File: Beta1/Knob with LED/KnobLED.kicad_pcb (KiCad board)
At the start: 2 copper layers, 197.9 x 41 mm, 116 parts, among them U0 APA102C, U1 APA102C, U10 APA102C, U1000 MCP3008T-I/SL, U11 APA102C, U12 APA102C, U13 APA102C, U14 APA102C, U15 APA102C, U2 APA102C, U3 APA102C, U4 APA102C, U5 APA102C, U6 APA102C, U7 APA102C, U8 APA102C, U9 APA102C

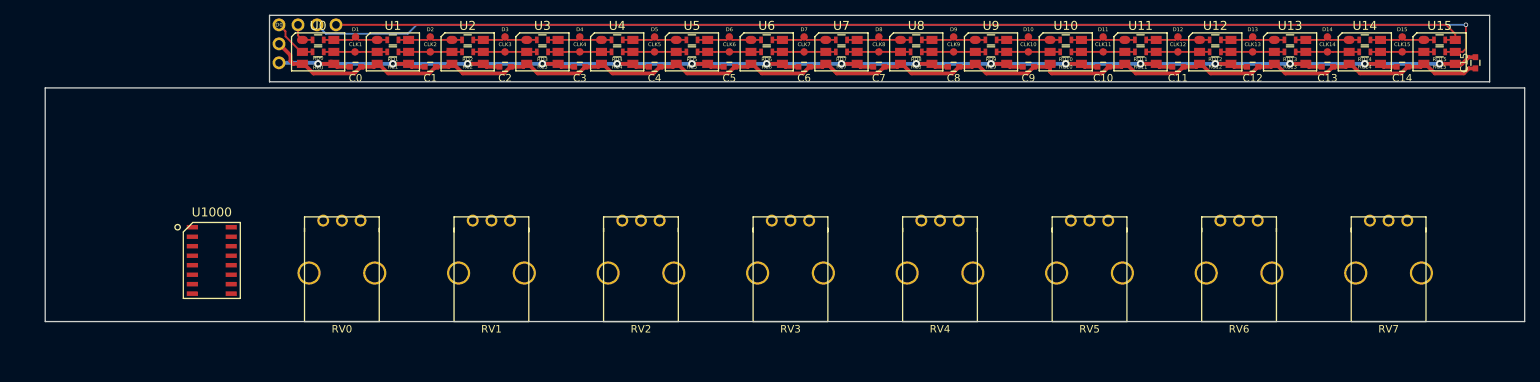
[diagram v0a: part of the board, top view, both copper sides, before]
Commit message: Fixed a math error and adjusted height of led board + component heights
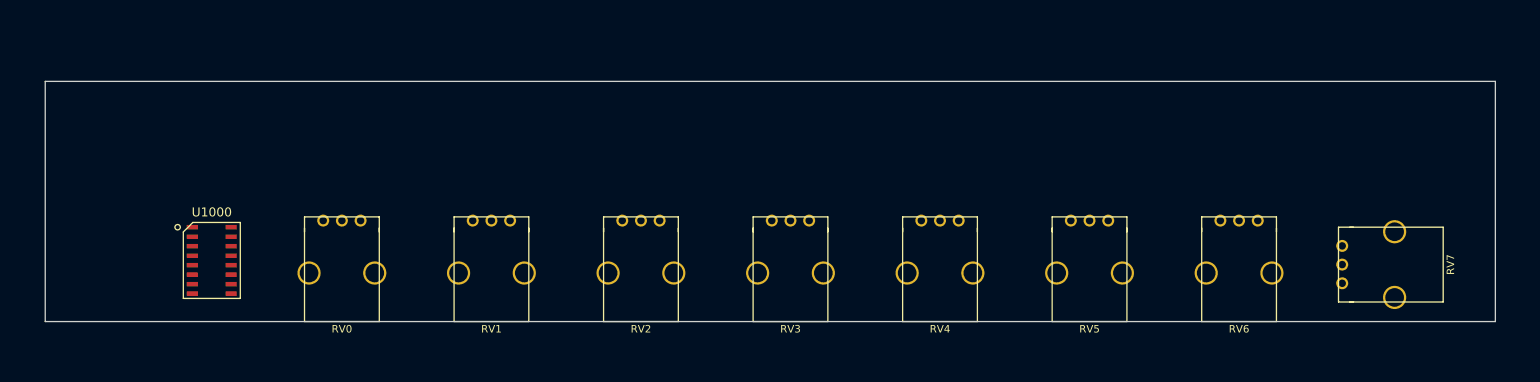
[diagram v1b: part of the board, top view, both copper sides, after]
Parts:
- removed C0, C1, C10, C11, C12, C13, C14, C15, C2, C3, C4, C5, C6, C7, C8, C9: 0.1u, Capacitors_SMD:C_0603
- removed CLK0, CLKOUT1, D0, DOUT1, GND0, VCC0: CONN_01X01, Liberry:single_0.1
- removed CLK1, CLK10, CLK11, CLK12, CLK13, CLK14, CLK15, CLK2, CLK3, CLK4, CLK5, CLK6, CLK7, CLK8, CLK9, D1, D10, D11, D12, D13, D14, D15, D2, D3, D4, D5, D6, D7, D8, D9: CONN_01X01, Liberry:TESTPAD
- removed RC0, RC1, RC10, RC11, RC12, RC13, RC14, RC15, RC2, RC3, RC4, RC5, RC6, RC7, RC8, RC9, RD0, RD1, RD10, RD11, RD12, RD13, RD14, RD15, RD2, RD3, RD4, RD5, RD6, RD7, RD8, RD9: ZERO, Resistors_SMD:R_0603
- removed U0, U1, U10, U11, U12, U13, U14, U15, U2, U3, U4, U5, U6, U7, U8, U9: APA102C, Liberry:PLCC6-1.6x4.2_LED
- moved RV7 3.60 mm to (177.0, -7.62), turned to 270 degrees
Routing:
- net +5V: track 227.1 -> 0.00 mm, vias 16 -> 0
- net GND: track 179.6 -> 0.00 mm
- net /LED_Strip/CLK16: track 160.8 -> 0.00 mm, vias 1 -> 0
- net /LED_Strip/D16: track 152.6 -> 0.00 mm
- net Net-(D1-Pad1): track 9.02 -> 0.00 mm
- net Net-(D3-Pad1): track 8.83 -> 0.00 mm
- net Net-(D2-Pad1): track 8.83 -> 0.00 mm
- net Net-(D9-Pad1): track 8.83 -> 0.00 mm
- net Net-(D7-Pad1): track 8.83 -> 0.00 mm
- net Net-(D6-Pad1): track 8.83 -> 0.00 mm
- net Net-(D5-Pad1): track 8.83 -> 0.00 mm
- net Net-(D15-Pad1): track 8.83 -> 0.00 mm
- net Net-(D14-Pad1): track 8.83 -> 0.00 mm
- net Net-(D13-Pad1): track 8.83 -> 0.00 mm
- net Net-(D11-Pad1): track 8.83 -> 0.00 mm
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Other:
- board size 197.9 x 41 mm -> 194 x 32.1 mm

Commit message: Duplicated row. Placed components and drill holes. Ready to be routed.
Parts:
- removed SPI_CS1: CONN_01X01, Liberry:single_0.1
- added C2: 0.1u, Capacitors_SMD:C_0603, F.Cu at (9.41, -9.34)
- added MISO2: CONN_01X01, Liberry:single_0.1, F.Cu at (7.62, -6.80)
- added REF**: 1pin, Connect:1pin, F.Cu at (3.00, -3.00)
- added REF**: 1pin, Connect:1pin, F.Cu at (3.00, -29.1)
- added REF**: 1pin, Connect:1pin, F.Cu at (191.0, -3.00)
- added REF**: 1pin, Connect:1pin, F.Cu at (191.0, -29.1)
- added RV10: POT, Liberry:RV09AF-40-20K-B10K, F.Cu at (75.8, -8.03)
- added RV11: POT, Liberry:RV09AF-40-20K-B10K, F.Cu at (95.8, -8.03)
- added RV12: POT, Liberry:RV09AF-40-20K-B10K, F.Cu at (115.8, -8.03)
- added RV13: POT, Liberry:RV09AF-40-20K-B10K, F.Cu at (135.8, -8.03)
- added RV14: POT, Liberry:RV09AF-40-20K-B10K, F.Cu at (155.8, -8.03)
- added RV15: POT, Liberry:RV09AF-40-20K-B10K, F.Cu at (175.8, -8.03)
- added RV8: POT, Liberry:RV09AF-40-20K-B10K, F.Cu at (35.8, -8.03)
- added RV9: POT, Liberry:RV09AF-40-20K-B10K, F.Cu at (55.8, -8.03)
- added SPI_CS_0_8: CONN_01X01, Liberry:single_0.1, F.Cu at (7.62, -28.8)
- added SPI_CS_8_15: CONN_01X01, Liberry:single_0.1, F.Cu at (7.62, -9.34)
- added U2: MCP3008T-I/SL, Liberry:SOIC-16, F.Cu at (15.8, -8.03)
- moved C1000 56.5 mm to (10.9, -23.7)
- moved SPICLK1 54.1 mm to (7.62, -31.3)
- moved MISO1 49.1 mm to (7.62, -26.2)
- moved MOSI1 43.8 mm to (7.62, -23.7)
- moved GND1000 43.4 mm to (7.62, -21.1)
- moved +3.3V1 38.1 mm to (7.62, -1.72)
- moved U1000 17.3 mm to (15.8, -24.2), turned to 90 degrees
- moved RV7 16.5 mm to (175.8, -24.1)
- moved RV5 14.6 mm to (135.8, -24.1), turned to 270 degrees
- moved RV6 14.6 mm to (155.8, -24.1), turned to 270 degrees
- moved RV0 14.6 mm to (35.8, -24.1), turned to 270 degrees
- moved RV1 14.6 mm to (55.8, -24.1), turned to 270 degrees
- moved RV2 14.6 mm to (75.8, -24.1), turned to 270 degrees
- moved RV3 14.6 mm to (95.8, -24.1), turned to 270 degrees
- moved RV4 14.6 mm to (115.8, -24.1), turned to 270 degrees
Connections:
- net Net-(MOSI1-Pad1) renamed /Knobs/MOSI
- net Net-(SPICLK1-Pad1) renamed /Knobs/SPICLK
- U1000 pad 10: Net-(SPI_CS1-Pad1) -> /Knobs/CS_R0_7
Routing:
- net (no net): track 203.5 -> 235.6 mm

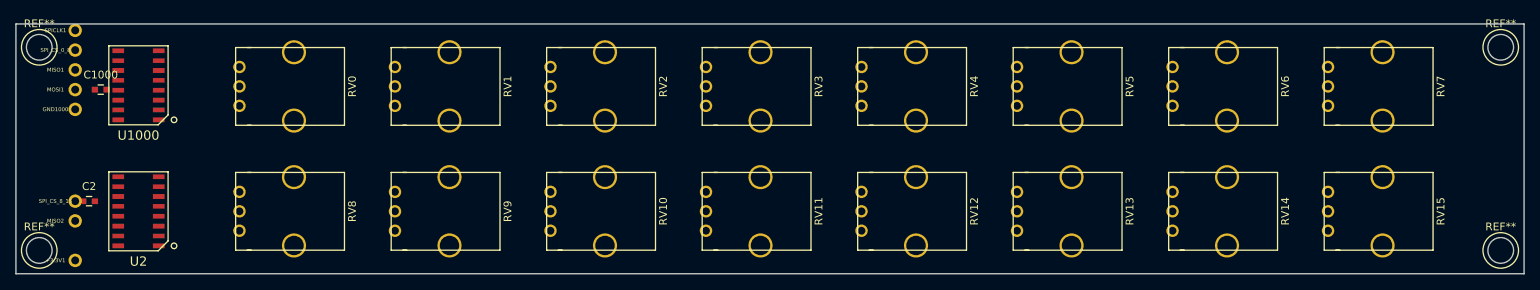
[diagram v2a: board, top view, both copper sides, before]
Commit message: Knob PCB is routed.
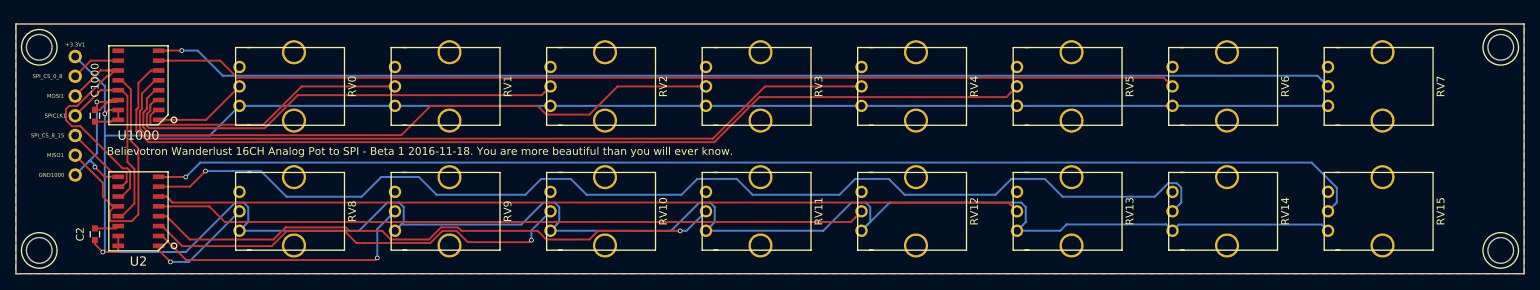
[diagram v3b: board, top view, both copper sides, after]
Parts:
- removed MISO2: CONN_01X01, Liberry:single_0.1
- moved +3.3V1 26.2 mm to (7.62, -27.9)
- moved SPICLK1 11.0 mm to (7.62, -20.3)
- moved MISO1 11.0 mm to (7.62, -15.2)
- moved GND1000 8.44 mm to (7.62, -12.7)
- moved SPI_CS_8_15 8.44 mm to (7.62, -17.8)
- moved C2 4.32 mm to (10.2, -5.08), turned to 90 degrees
- moved C1000 3.45 mm to (10.2, -20.3), turned to 90 degrees
- moved SPI_CS_0_8 3.36 mm to (7.62, -25.4)
- moved MOSI1 0.82 mm to (7.62, -22.9)
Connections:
- MISO1 pad 1: Net-(MISO1-Pad1) -> /Knobs/MISO
- U1000 pad 12: Net-(MISO1-Pad1) -> /Knobs/MISO
- U2 pad 12: Net-(MISO2-Pad1) -> /Knobs/MISO
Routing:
- net +3V3: track 0.00 -> 395.1 mm, vias 0 -> 2
- net /Knobs/P15: track 0.00 -> 157.1 mm, vias 0 -> 1
- net /Knobs/P7: track 0.00 -> 152.3 mm, vias 0 -> 1
- net /Knobs/P14: track 0.00 -> 147.0 mm, vias 0 -> 1
- net /Knobs/P6: track 0.00 -> 131.8 mm
- net /Knobs/P5: track 0.00 -> 126.4 mm
- net /Knobs/P13: track 0.00 -> 111.2 mm
- net /Knobs/P4: track 0.00 -> 103.6 mm
- net /Knobs/P12: track 0.00 -> 91.8 mm
- net /Knobs/P3: track 0.00 -> 82.1 mm
- net /Knobs/P11: track 0.00 -> 75.7 mm, vias 0 -> 1
- net /Knobs/P2: track 0.00 -> 58.5 mm
- net /Knobs/P10: track 0.00 -> 56.5 mm, vias 0 -> 1
- net /Knobs/P9: track 0.00 -> 36.5 mm, vias 0 -> 1
- net /Knobs/P1: track 0.00 -> 36.0 mm
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- added copper zone on F.Cu, net GND
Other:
- board text added: "Believotron Wanderlust 16CH Analog Pot to SPI - Beta 1 2016-11-18. You are more beautiful than you will ever know."
